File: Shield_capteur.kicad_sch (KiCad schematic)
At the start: 19 parts, among them J1 Power, J2 Digital/PWM, J3 Analog, J4 Digital/PWM, K63 1uF, U1 LTC1050ACN8_PBF, U2 MCP

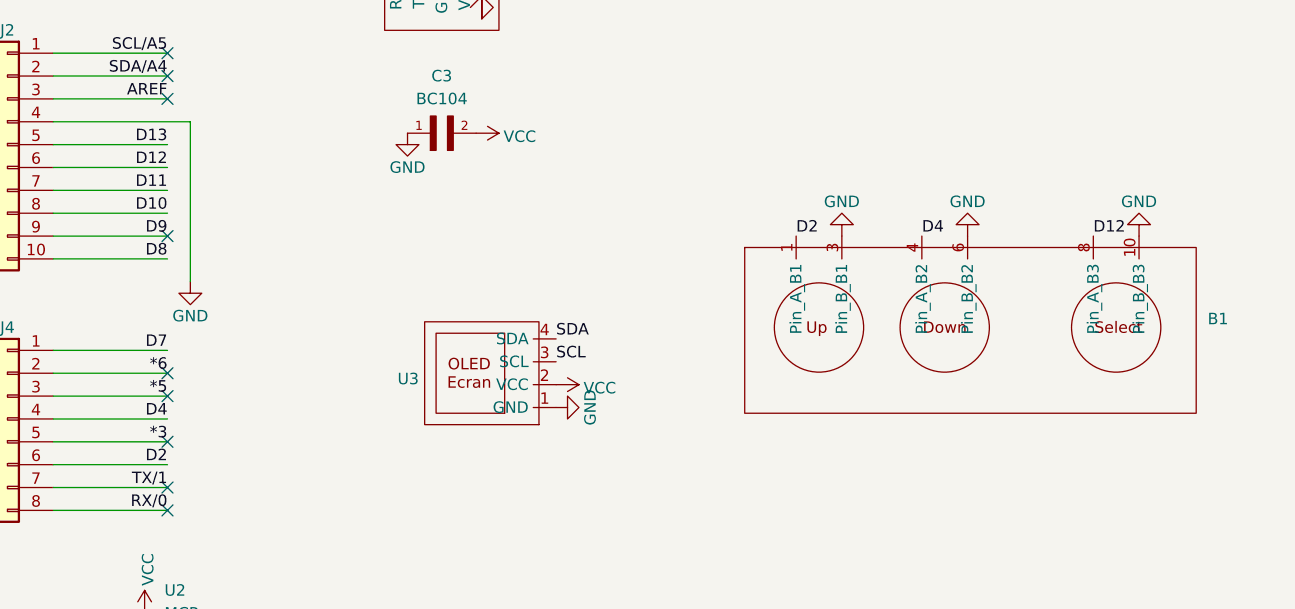
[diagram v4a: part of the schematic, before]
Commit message: Fin du placement des composants et pistes sur PCB. Quelques erreurs mineures à régler
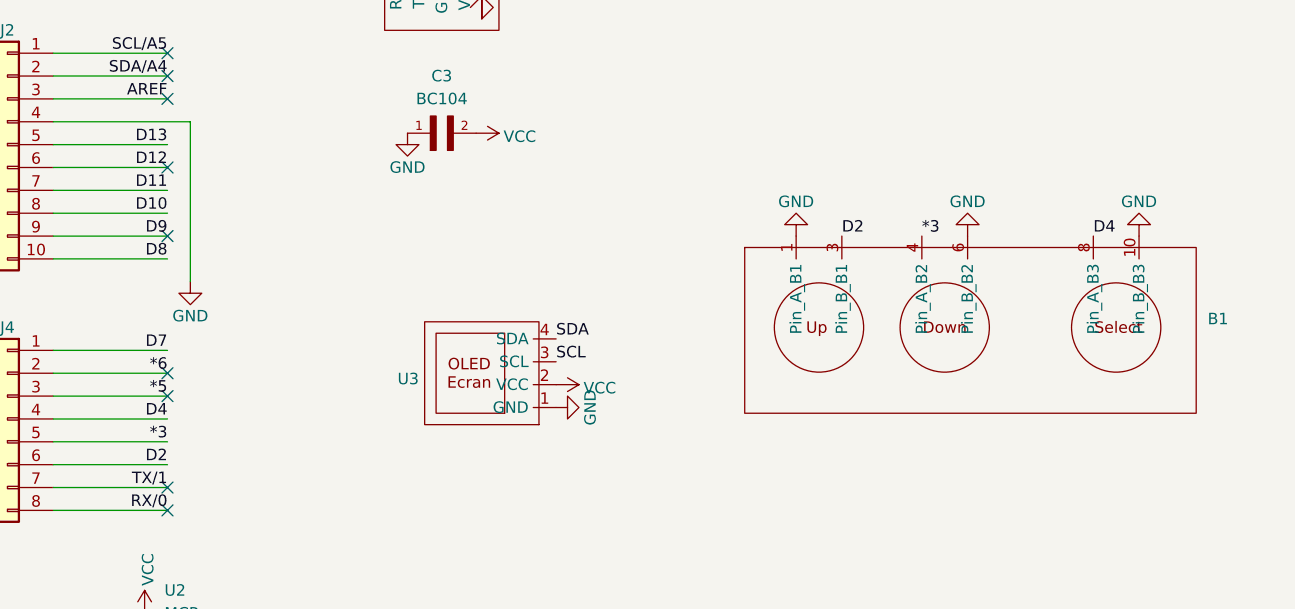
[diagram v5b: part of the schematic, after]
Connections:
- net *3: now also B1.4 (Pin_A_B2)
- net D12: no longer B1.8 (Pin_A_B3)
- net D2: now also B1.3 (Pin_B_B1); no longer B1.1 (Pin_A_B1)
- net D4: now also B1.8 (Pin_A_B3); no longer B1.4 (Pin_A_B2)
- net GND: now also B1.1 (Pin_A_B1); no longer B1.3 (Pin_B_B1)
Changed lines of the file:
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@@
+	)
+	(no_connect
+		(at 100.33 53.34)
 	)
 	(no_connect
@@
 	(no_connect
 		(at 100.33 88.9)
-	)
-	(no_connect
-		(at 100.33 83.82)
 	)
 	(no_connect
@@
 		)
 	)
-	(label "D12"
+	(label "D4"
 		(at 203.2 60.96 0)
 		(fields_autoplaced yes)
@@
 		)
 	)
-	(label "D4"
+	(label "*3"
 		(at 184.15 60.96 0)
 		(fields_autoplaced yes)
@@
 	)
 	(label "D2"
-		(at 170.18 60.96 0)
+		(at 175.26 60.96 0)
 		(fields_autoplaced yes)
 		(effects
@@
 	(symbol
 		(lib_id "power:GND")
-		(at 175.26 60.96 180)
+		(at 170.18 60.96 180)
 		(unit 1)
 		(exclude_from_sim no)
@@
 		(dnp no)
 		(property "Reference" "#PWR022"
-			(at 175.26 54.61 0)
+			(at 170.18 54.61 0)
 			(effects
 				(font
@@
 		)
 		(property "Value" "GND"
-			(at 175.26 57.15 0)
+			(at 170.18 57.15 0)
 			(effects
 				(font
@@
 		)
 		(property "Footprint" ""
-			(at 175.26 60.96 0)
+			(at 170.18 60.96 0)
 			(effects
 				(font
@@
 		)
 		(property "Datasheet" ""
-			(at 175.26 60.96 0)
+			(at 170.18 60.96 0)
 			(effects
 				(font
@@
 		)
 		(property "Description" "Power symbol creates a global label with name \"GND\" , ground"
-			(at 175.26 60.96 0)
-			(effects
-				(font
+			(at 170.18 60.96 0)
+			(effects
+				(font

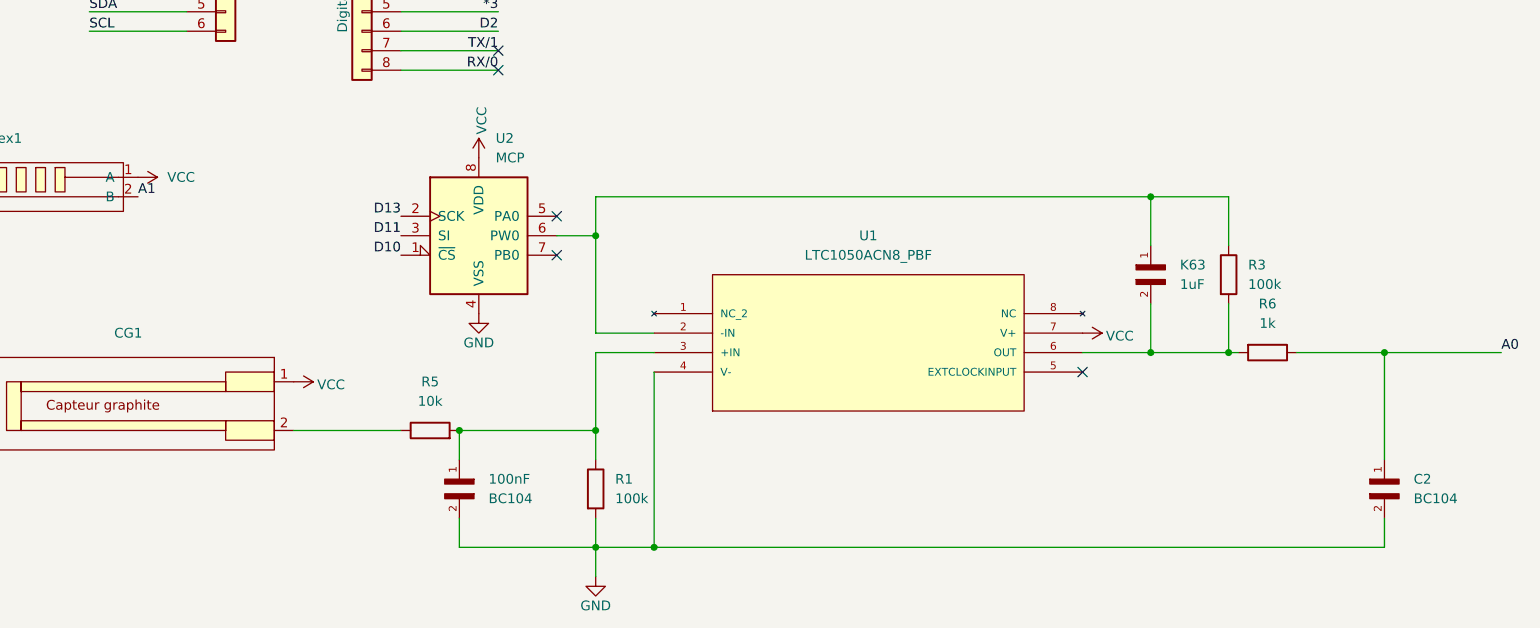
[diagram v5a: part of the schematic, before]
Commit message: Correction du PCB il reste connection RFlex
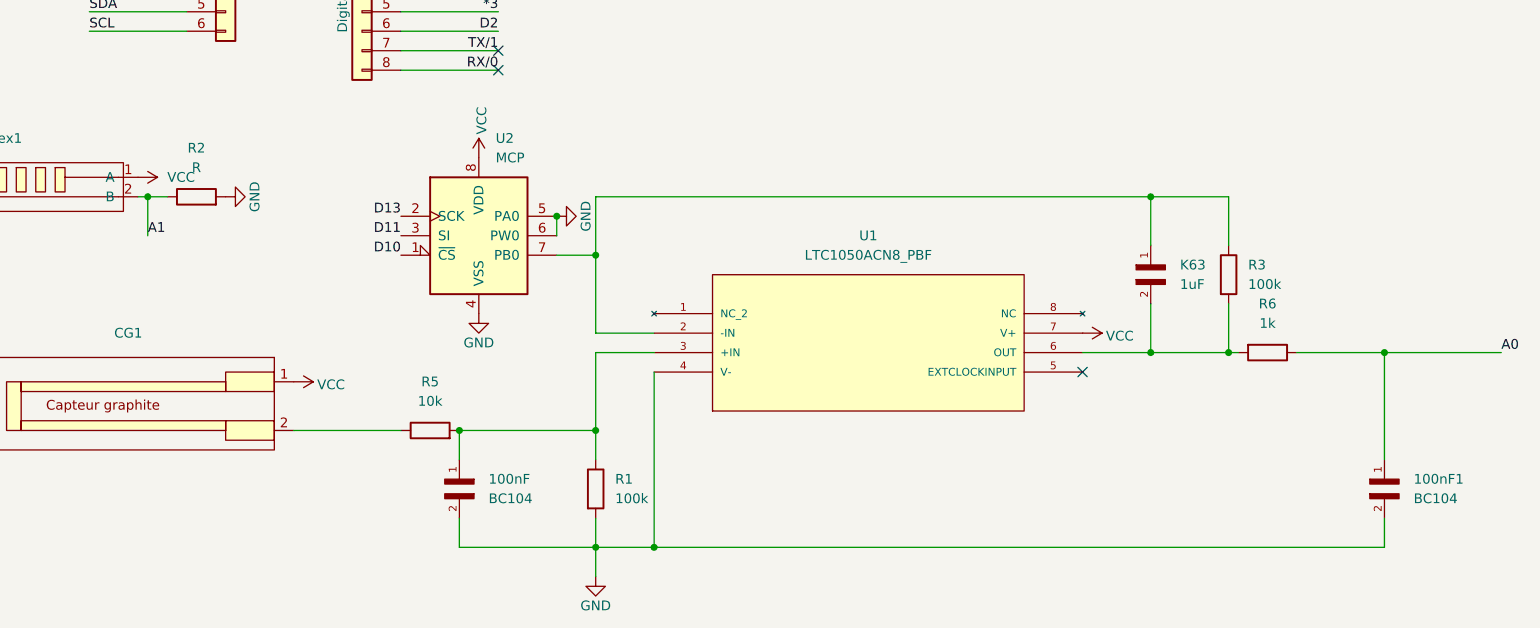
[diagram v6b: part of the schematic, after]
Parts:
- added R2: R, Resistor_THT:R_Axial_DIN0207_L6.3mm_D2.5mm_P10.16mm_Horizontal, symbol Device:R
- renumbered C2 to 100nF1
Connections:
- net A1: now also R2.1
- net GND: now also U2.5 (PA0), U2.6 (PW0), R2.2
- net at K63.1, R3.1, U1.2 (-IN): now also U2.7 (PB0); no longer U2.6 (PW0)
- no-connect marks 17 -> 15

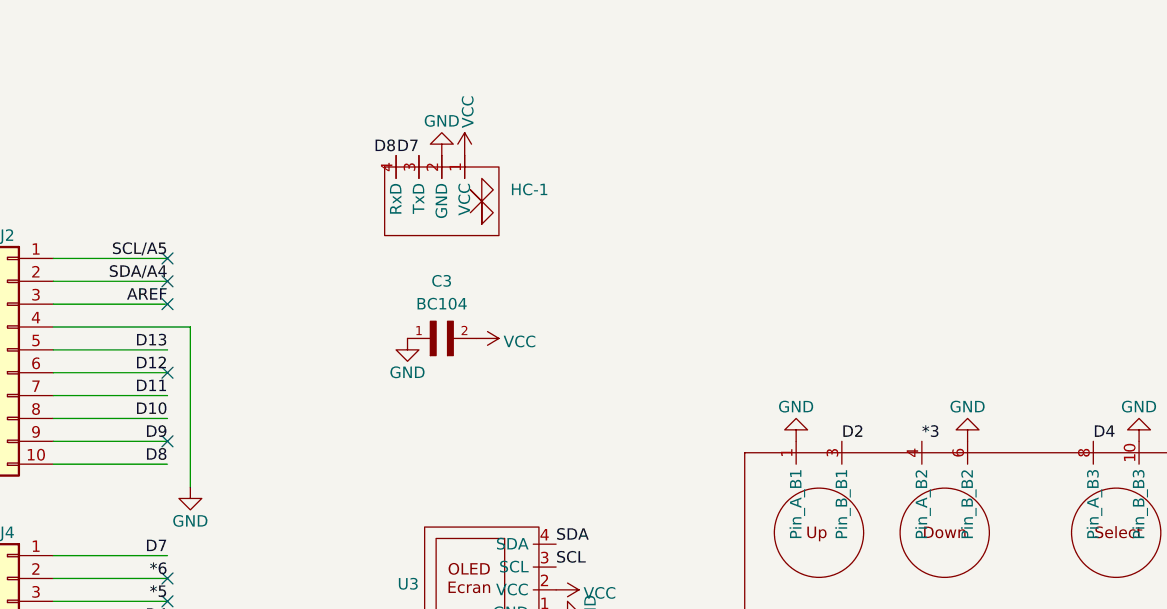
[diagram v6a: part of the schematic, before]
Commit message: Ajout lien second Arduino
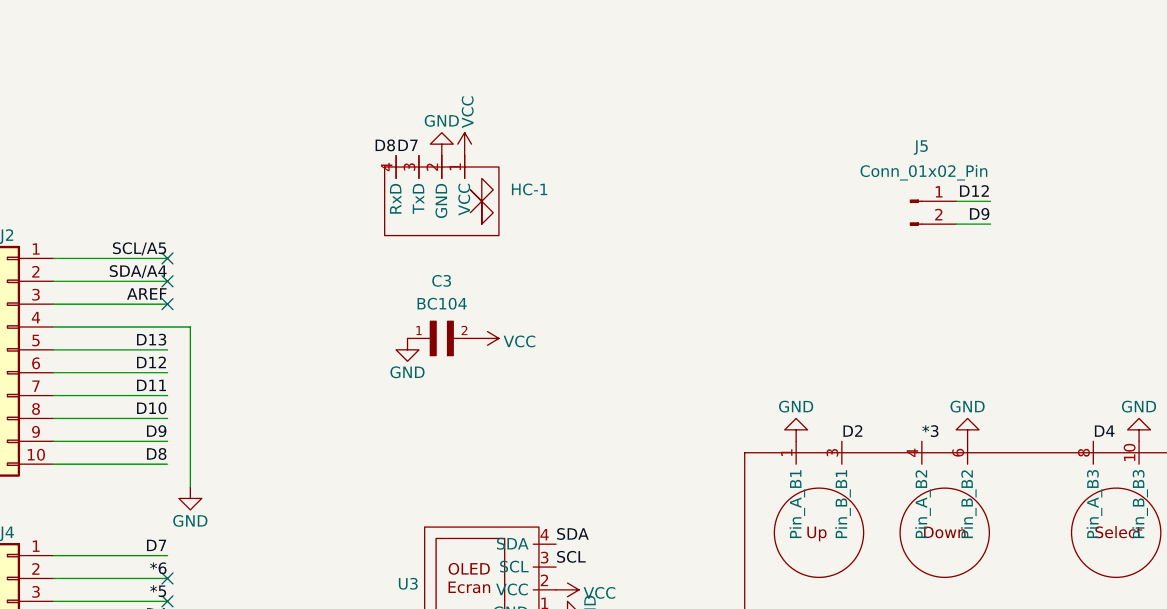
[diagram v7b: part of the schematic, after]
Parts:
- added J5: Conn_01x02_Pin, Connector_PinSocket_2.54mm:PinSocket_1x02_P2.54mm_Vertical, symbol Connector:Conn_01x02_Pin
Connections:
- net D12: now also J5.1 (Pin_1)
- net D9: now also J5.2 (Pin_2)
- no-connect marks 15 -> 13
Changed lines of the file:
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@@
 	)
 	(no_connect
-		(at 100.33 53.34)
-	)
-	(no_connect
 		(at 176.53 130.81)
 	)
@@
 	)
 	(no_connect
-		(at 100.33 60.96)
-	)
-	(no_connect
 		(at 44.45 50.8)
 	)
@@
 	(wire
 		(pts
+			(xy 191.77 34.29) (xy 187.96 34.29)
+		)
+		(stroke
+			(width 0)
+			(type default)
+		)
+	)
+	(wire
+		(pts
 			(xy 195.58 121.92) (xy 195.58 128.27)
 		)
@@
 	(wire
 		(pts
+			(xy 191.77 36.83) (xy 187.96 36.83)
+		)
+		(stroke
+			(width 0)
+			(type default)
+		)
+	)
+	(wire
+		(pts
 			(xy 87.63 88.9) (xy 100.33 88.9)
 		)
@@
 		)
 	)
+	(label "D12"
+		(at 191.77 34.29 180)
+		(fields_autoplaced yes)
+		(effects
+			(font
+				(size 1.27 1.27)
+			)
+			(justify right bottom)
+		)
+	)
 	(label "SCL"
 		(at 143.51 74.93 0)
@@
 		)
 	)
+	(label "D9"
+		(at 191.77 36.83 180)
+		(fields_autoplaced yes)
+		(effects
+			(font
+				(size 1.27 1.27)
+			)
+			(justify right bottom)
+		)
+	)
 	(label "AREF"
 		(at 100.33 45.72 180)
@@
 					(unit 1)
 				)
+			)
+		)
+	)
+	(symbol
+		(lib_id "Connector:Conn_01x02_Pin")
+		(at 182.88 34.29 0)
+		(unit 1)
+		(exclude_from_sim no)
+		(in_bom yes)
+		(on_board yes)
+		(dnp no)
+		(property "Reference" "J5"
+			(at 184.15 28.194 0)
+			(effects
+				(font
+					(size 1.27 1.27)
+				)
+			)
+		)
+		(property "Value" "Conn_01x02_Pin"
+			(at 184.404 30.988 0)
+			(effects
+				(font
+					(size 1.27 1.27)
+				)
+			)
+		)
+		(property "Footprint" "Connector_PinSocket_2.54mm:PinSocket_1x02_P2.54mm_Vertical"
+			(at 182.88 34.29 0)
+			(effects
+				(font
+					(size 1.27 1.27)
+				)
+				(hide yes)
+			)
+		)
+		(property "Datasheet" "~"
+			(at 182.88 34.29 0)
+			(effects
+				(font
+					(size 1.27 1.27)
+				)
+				(hide yes)
+			)
+		)
+		(property "Description" "Generic connector, single row, 01x02, script generated"
+			(at 182.88 34.29 0)
+			(effects
+				(font
+					(size 1.27 1.27)
+				)
+				(hide yes)
+			)
+		)
+		(pin "2"
+		)
+		(pin "1"
+		)
+		(instances
+			(project "Shield_capteur"
+				(path "/e63e39d7-6ac0-4ffd-8aa3-1841a4541b55"
+					(reference "J5")
+					(unit 1)
+				)

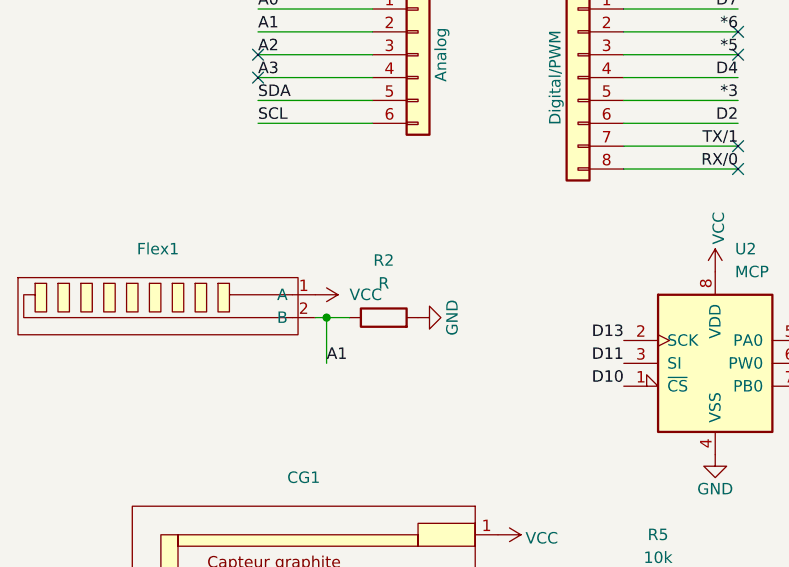
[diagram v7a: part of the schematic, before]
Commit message: fin kicad ajout liaison second arduino
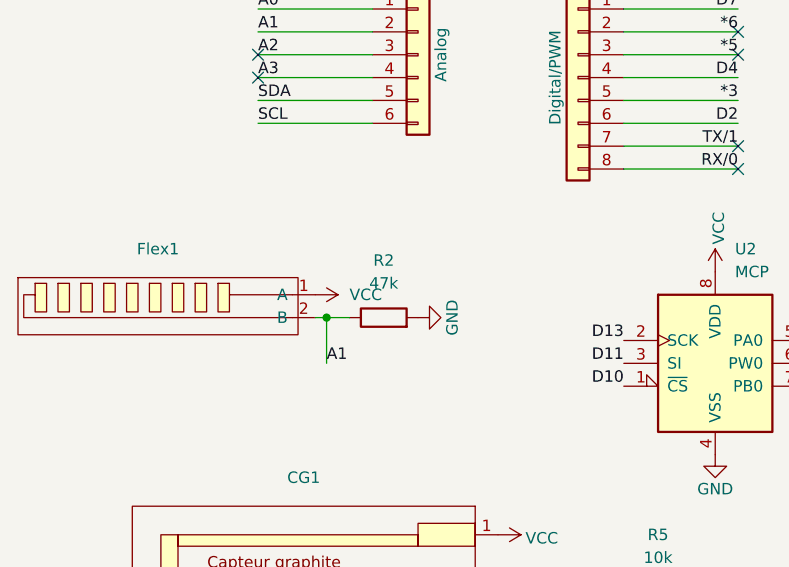
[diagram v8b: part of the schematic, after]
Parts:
- R2: value R -> 47k
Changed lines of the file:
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@@
 			)
 		)
-		(property "Value" "R"
+		(property "Value" "47k"
 			(at 60.96 104.14 90)
 			(effects
